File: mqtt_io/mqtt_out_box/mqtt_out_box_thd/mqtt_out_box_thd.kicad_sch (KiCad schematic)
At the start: 63 parts, among them J1 Conn_01x02, J3 Conn_01x04_Pin, K1 FINDER-40.52, K2 FINDER-40.52, K3 FINDER-40.52, K4 FINDER-40.52, K5 FINDER-40.52, K6 FINDER-40.52, K7 FINDER-40.52, K8 FINDER-40.52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

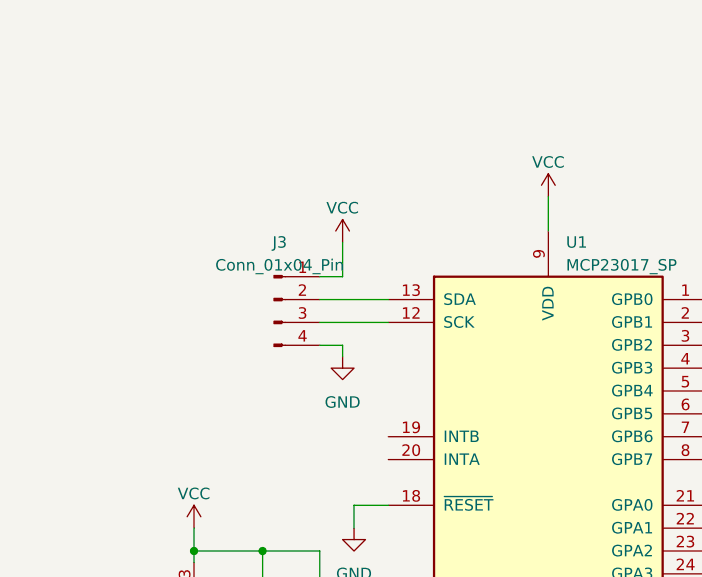
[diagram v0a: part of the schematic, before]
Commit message: Pullup für ic2 eingefügt (4k7)
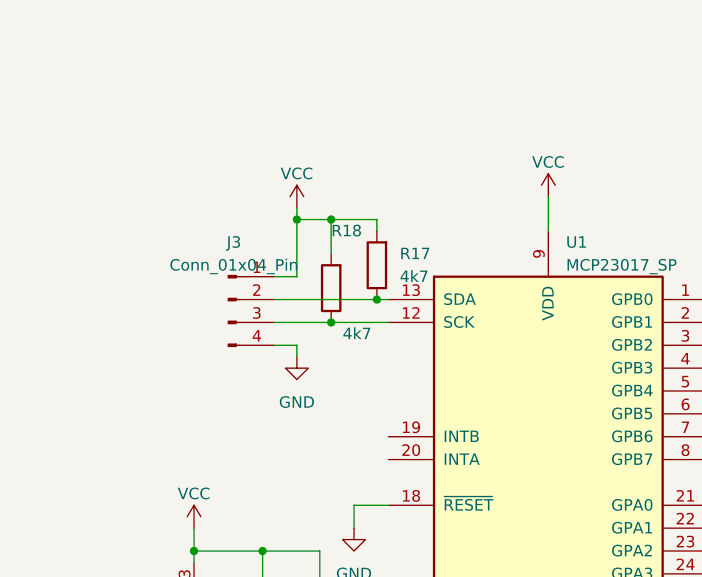
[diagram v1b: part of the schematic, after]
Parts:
- added R17, R18: 4k7, Resistor_THT:R_Axial_DIN0204_L3.6mm_D1.6mm_P7.62mm_Horizontal, symbol Device:R
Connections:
- net VCC: now also R17.2, R18.2
- net at J3.3 (Pin_3), U1.12 (SCK): now also R18.1
- net at J3.2 (Pin_2), U1.13 (SDA): now also R17.1
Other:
- moved on the sheet: J3
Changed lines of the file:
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@@
   (junction (at 95.25 171.45) (diameter 0) (color 0 0 0 0)
   )
+  (junction (at 44.45 63.5) (diameter 0) (color 0 0 0 0)
+  )
   (junction (at 146.05 91.44) (diameter 0) (color 0 0 0 0)
   )
@@
   (junction (at 36.83 88.9) (diameter 0) (color 0 0 0 0)
   )
+  (junction (at 49.53 60.96) (diameter 0) (color 0 0 0 0)
+  )
   (junction (at 242.57 77.47) (diameter 0) (color 0 0 0 0)
   )
@@
   (junction (at 95.25 144.78) (diameter 0) (color 0 0 0 0)
   )
+  (junction (at 44.45 52.07) (diameter 0) (color 0 0 0 0)
+  )
+  (junction (at 40.64 52.07) (diameter 0) (color 0 0 0 0)
+  )
   (junction (at 196.85 26.67) (diameter 0) (color 0 0 0 0)
   )
@@
     (stroke (width 0) (type default))
   )
+  (wire (pts (xy 49.53 53.34) (xy 49.53 52.07))
+    (stroke (width 0) (type default))
+  )
   (wire (pts (xy 242.57 59.69) (xy 227.33 59.69))
     (stroke (width 0) (type default))
@@
     (stroke (width 0) (type default))
   )
+  (wire (pts (xy 44.45 52.07) (xy 44.45 55.88))
+    (stroke (width 0) (type default))
+  )
   (wire (pts (xy 196.85 71.12) (xy 214.63 71.12))
     (stroke (width 0) (type default))
@@
     (stroke (width 0) (type default))
   )
-  (wire (pts (xy 43.18 58.42) (xy 45.72 58.42))
+  (wire (pts (xy 38.1 58.42) (xy 40.64 58.42))
     (stroke (width 0) (type default))
   )
@@
     (stroke (width 0) (type default))
   )
-  (wire (pts (xy 45.72 66.04) (xy 45.72 67.31))
+  (wire (pts (xy 40.64 66.04) (xy 40.64 67.31))
     (stroke (width 0) (type default))
   )
@@
     (stroke (width 0) (type default))
   )
+  (wire (pts (xy 44.45 52.07) (xy 40.64 52.07))
+    (stroke (width 0) (type default))
+  )
   (wire (pts (xy 85.09 173.99) (xy 95.25 173.99))
     (stroke (width 0) (type default))
@@
     (stroke (width 0) (type default))
   )
-  (wire (pts (xy 43.18 63.5) (xy 50.8 63.5))
+  (wire (pts (xy 38.1 63.5) (xy 44.45 63.5))
     (stroke (width 0) (type default))
   )
@@
     (stroke (width 0) (type default))
   )
+  (wire (pts (xy 49.53 52.07) (xy 44.45 52.07))
+    (stroke (width 0) (type default))
+  )
   (wire (pts (xy 29.21 102.87) (xy 29.21 111.76))
     (stroke (width 0) (type default))
@@
     (stroke (width 0) (type default))
   )
+  (wire (pts (xy 49.53 60.96) (xy 50.8 60.96))
+    (stroke (width 0) (type default))
+  )
   (wire (pts (xy 196.85 138.43) (xy 196.85 142.24))
     (stroke (width 0) (type default))
@@
     (stroke (width 0) (type default))
   )
+  (wire (pts (xy 44.45 63.5) (xy 50.8 63.5))
+    (stroke (width 0) (type default))
+  )
   (wire (pts (xy 43.18 88.9) (xy 36.83 88.9))
     (stroke (width 0) (type default))
@@
     (stroke (width 0) (type default))
   )
+  (wire (pts (xy 40.64 52.07) (xy 40.64 58.42))
+    (stroke (width 0) (type default))
+  )
   (wire (pts (xy 274.32 36.83) (xy 278.13 36.83))
     (stroke (width 0) (type default))
@@
     (stroke (width 0) (type default))
   )
-  (wire (pts (xy 45.72 54.61) (xy 45.72 58.42))
-    (stroke (width 0) (type default))
-  )
-  (wire (pts (xy 43.18 60.96) (xy 50.8 60.96))
+  (wire (pts (xy 40.64 50.8) (xy 40.64 52.07))
+    (stroke (width 0) (type default))
+  )
+  (wire (pts (xy 38.1 60.96) (xy 49.53 60.96))
     (stroke (width 0) (type default))
   )
@@
     (stroke (width 0) (type default))
   )
-  (wire (pts (xy 43.18 66.04) (xy 45.72 66.04))
+  (wire (pts (xy 38.1 66.04) (xy 40.64 66.04))
     (stroke (width 0) (type default))
   )
@@
     )
   )
-  (symbol (lib_id "power:VCC") (at 45.72 54.61 0) (unit 1)
-    (in_bom yes) (on_board yes) (dnp no) (fields_autoplaced)
-    (property "Reference" "#PWR07" (at 45.72 58.42 0)
-      (effects (font (size 1.27 1.27)) hide)
-    )
-    (property "Value" "VCC" (at 45.72 50.8 0)
-      (effects (font (size 1.27 1.27)))
-    )
-    (property "Footprint" "" (at 45.72 54.61 0)
-      (effects (font (size 1.27 1.27)) hide)
-    )
-    (property "Datasheet" "" (at 45.72 54.61 0)
+  (symbol (lib_id "power:VCC") (at 40.64 50.8 0) (unit 1)
+    (in_bom yes) (on_board yes) (dnp no) (fields_autoplaced)
+    (property "Reference" "#PWR07" (at 40.64 54.61 0)
+      (effects (font (size 1.27 1.27)) hide)
+    )
+    (property "Value" "VCC" (at 40.64 46.99 0)
+      (effects (font (size 1.27 1.27)))
+    )
+    (property "Footprint" "" (at 40.64 50.8 0)
+      (effects (font (size 1.27 1.27)) hide)
+    )
+    (property "Datasheet" "" (at 40.64 50.8 0)
       (effects (font (size 1.27 1.27)) hide)
     )
@@
     )
   )
+  (symbol (lib_id "Device:R") (at 49.53 57.15 180) (unit 1)
+    (in_bom yes) (on_board yes) (dnp no)
+    (property "Reference" "R17" (at 52.07 55.88 0)
+      (effects (font (size 1.27 1.27)) (justify right))
+    )
+    (property "Value" "4k7" (at 52.07 58.42 0)
+      (effects (font (size 1.27 1.27)) (justify right))
+    )
+    (property "Footprint" "Resistor_THT:R_Axial_DIN0204_L3.6mm_D1.6mm_P7.62mm_Horizontal" (at 51.308 57.15 90)
+      (effects (font (size 1.27 1.27)) hide)
+    )
+    (property "Datasheet" "~" (at 49.53 57.15 0)
+      (effects (font (size 1.27 1.27)) hide)
+    )
+    (pin "1")
+    (pin "2")
+    (instances
+      (project "mqtt_out_box_thd"
+        (path "/34176d03-642b-4b4b-a78a-29d577408e6d"
+          (reference "R17") (unit 1)
+        )
+      )
+      (project "mqtt_out_box"
+        (path "/d6a7dd6e-fa52-4ea7-ba98-8f1dfc1763a3"
+          (reference "R1") (unit 1)
+        )
+      )
+    )
+  )
   (symbol (lib_id "Device:R") (at 97.79 73.66 90) (unit 1)
     (in_bom yes) (on_board yes) (dnp no) (fields_autoplaced)
@@
     )
   )
-  (symbol (lib_id "Connector:Conn_01x04_Pin") (at 38.1 60.96 0) (unit 1)
+  (symbol (lib_id "Connector:Conn_01x04_Pin") (at 33.02 60.96 0) (unit 1)
     (in_bom yes) (on_board yes) (dnp no)
-    (property "Reference" "J3" (at 38.735 54.61 0)
-      (effects (font (size 1.27 1.27)))
-    )
-    (property "Value" "Conn_01x04_Pin" (at 38.735 57.15 0)
-      (effects (font (size 1.27 1.27)))
-    )
-    (property "Footprint" "Connector_PinHeader_2.54mm:PinHeader_1x04_P2.54mm_Vertical" (at 38.1 60.96 0)
-      (effects (font (size 1.27 1.27)) hide)
-    )
-    (property "Datasheet" "~" (at 38.1 60.96 0)
+    (property "Reference" "J3" (at 33.655 54.61 0)
+      (effects (font (size 1.27 1.27)))
+    )
+    (property "Value" "Conn_01x04_Pin" (at 33.655 57.15 0)
+      (effects (font (size 1.27 1.27)))
+    )
+    (property "Footprint" "Connector_PinHeader_2.54mm:PinHeader_1x04_P2.54mm_Vertical" (at 33.02 60.96 0)
+      (effects (font (size 1.27 1.27)) hide)
+    )
+    (property "Datasheet" "~" (at 33.02 60.96 0)
       (effects (font (size 1.27 1.27)) hide)
     )
@@
     )
   )
-  (symbol (lib_id "power:GND") (at 45.72 67.31 0) (unit 1)
-    (in_bom yes) (on_board yes) (dnp no) (fields_autoplaced)
-    (property "Reference" "#PWR09" (at 45.72 73.66 0)
-      (effects (font (size 1.27 1.27)) hide)
-    )
-    (property "Value" "GND" (at 45.72 72.39 0)
-      (effects (font (size 1.27 1.27)))
-    )
-    (property "Footprint" "" (at 45.72 67.31 0)
-      (effects (font (size 1.27 1.27)) hide)
-    )
-    (property "Datasheet" "" (at 45.72 67.31 0)
+  (symbol (lib_id "power:GND") (at 40.64 67.31 0) (unit 1)
+    (in_bom yes) (on_board yes) (dnp no) (fields_autoplaced)
+    (property "Reference" "#PWR09" (at 40.64 73.66 0)
+      (effects (font (size 1.27 1.27)) hide)
+    )
+    (property "Value" "GND" (at 40.64 72.39 0)
+      (effects (font (size 1.27 1.27)))
+    )
+    (property "Footprint" "" (at 40.64 67.31 0)
+      (effects (font (size 1.27 1.27)) hide)
+    )
+    (property "Datasheet" "" (at 40.64 67.31 0)
       (effects (font (size 1.27 1.27)) hide)
     )
@@
         )
       )
+    )
+  )
+  (symbol (lib_id "Device:R") (at 44.45 59.69 180) (unit 1)
+    (in_bom yes) (on_board yes) (dnp no)
+    (property "Reference" "R18" (at 44.45 53.34 0)
+      (effects (font (size 1.27 1.27)) (justify right))
+    )
+    (property "Value" "4k7" (at 45.72 64.77 0)
+      (effects (font (size 1.27 1.27)) (justify right))
+    )
+    (property "Footprint" "Resistor_THT:R_Axial_DIN0204_L3.6mm_D1.6mm_P7.62mm_Horizontal" (at 46.228 59.69 90)
+      (effects (font (size 1.27 1.27)) hide)
+    )
+    (property "Datasheet" "~" (at 44.45 59.69 0)
+      (effects (font (size 1.27 1.27)) hide)
+    )
+    (pin "1")
+    (pin "2")
+    (instances
+      (project "mqtt_out_box_thd"
+        (path "/34176d03-642b-4b4b-a78a-29d577408e6d"
+          (reference "R18") (unit 1)
+        )
+      )
+      (project "mqtt_out_box"
+        (path "/d6a7dd6e-fa52-4ea7-ba98-8f1dfc1763a3"
+          (reference "R1") (unit 1)
+        )
+      )

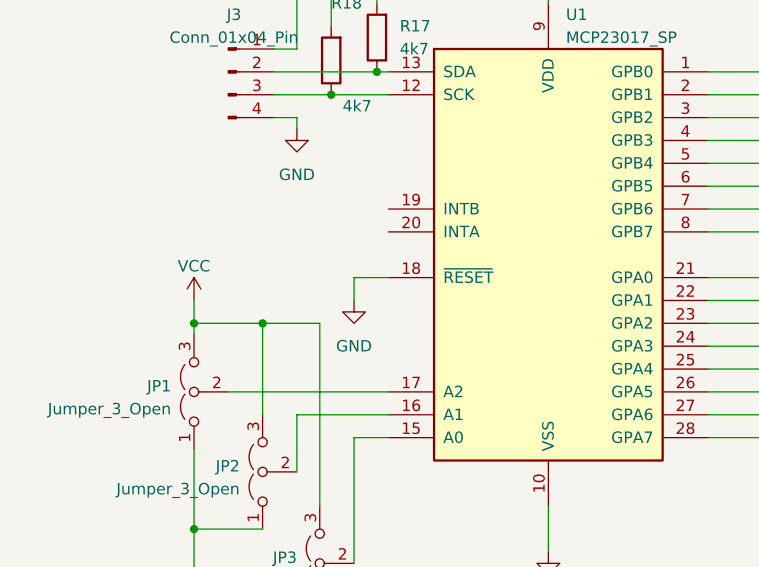
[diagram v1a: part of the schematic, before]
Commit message: neue Dateien eingefügt.
out Platine rev 2, testprogramm für pi pico
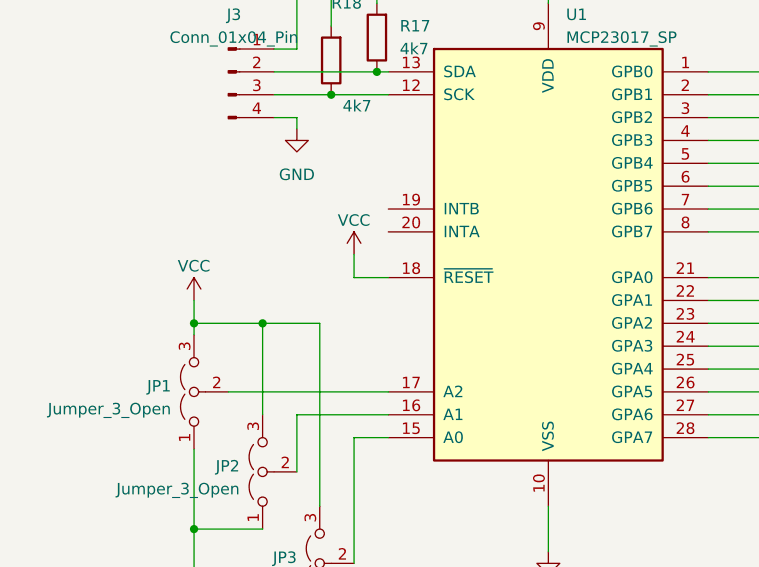
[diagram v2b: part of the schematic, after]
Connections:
- net GND: no longer U1.18 (~{RESET})
- net VCC: now also U1.18 (~{RESET})
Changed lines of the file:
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@@
     (stroke (width 0) (type default))
   )
+  (wire (pts (xy 46.99 81.28) (xy 46.99 83.82))
+    (stroke (width 0) (type default))
+  )
   (wire (pts (xy 232.41 134.62) (xy 232.41 139.7))
     (stroke (width 0) (type default))
@@
     (stroke (width 0) (type default))
   )
-  (wire (pts (xy 46.99 83.82) (xy 46.99 86.36))
-    (stroke (width 0) (type default))
-  )
   (wire (pts (xy 207.01 97.79) (xy 227.33 97.79))
     (stroke (width 0) (type default))
@@
     )
   )
-  (symbol (lib_id "power:GND") (at 46.99 86.36 0) (unit 1)
-    (in_bom yes) (on_board yes) (dnp no) (fields_autoplaced)
-    (property "Reference" "#PWR013" (at 46.99 92.71 0)
-      (effects (font (size 1.27 1.27)) hide)
-    )
-    (property "Value" "GND" (at 46.99 91.44 0)
-      (effects (font (size 1.27 1.27)))
-    )
-    (property "Footprint" "" (at 46.99 86.36 0)
-      (effects (font (size 1.27 1.27)) hide)
-    )
-    (property "Datasheet" "" (at 46.99 86.36 0)
-      (effects (font (size 1.27 1.27)) hide)
-    )
-    (pin "1")
-    (instances
-      (project "mqtt_out_box_thd"
-        (path "/34176d03-642b-4b4b-a78a-29d577408e6d"
-          (reference "#PWR013") (unit 1)
-        )
-      )
-      (project "mqtt_out_box"
-        (path "/d6a7dd6e-fa52-4ea7-ba98-8f1dfc1763a3"
-          (reference "#PWR05") (unit 1)
-        )
-      )
-    )
-  )
   (symbol (lib_id "power:VCC") (at 68.58 49.53 0) (unit 1)
     (in_bom yes) (on_board yes) (dnp no) (fields_autoplaced)
@@
         )
       )
+    )
+  )
+  (symbol (lib_id "power:VCC") (at 46.99 81.28 0) (unit 1)
+    (in_bom yes) (on_board yes) (dnp no) (fields_autoplaced)
+    (property "Reference" "#PWR013" (at 46.99 85.09 0)
+      (effects (font (size 1.27 1.27)) hide)
+    )
+    (property "Value" "VCC" (at 46.99 77.47 0)
+      (effects (font (size 1.27 1.27)))
+    )
+    (property "Footprint" "" (at 46.99 81.28 0)
+      (effects (font (size 1.27 1.27)) hide)
+    )
+    (property "Datasheet" "" (at 46.99 81.28 0)
+      (effects (font (size 1.27 1.27)) hide)
+    )
+    (pin "1")
+    (instances
+      (project "mqtt_out_box_thd"
+        (path "/34176d03-642b-4b4b-a78a-29d577408e6d"
+          (reference "#PWR013") (unit 1)
+        )
+      )
+      (project "mqtt_out_box"
+        (path "/d6a7dd6e-fa52-4ea7-ba98-8f1dfc1763a3"
+          (reference "#PWR03") (unit 1)
+        )
+      )
